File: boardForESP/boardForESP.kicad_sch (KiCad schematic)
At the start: 6 parts, among them J1 Conn_01x15_Socket, J2 Conn_01x15_Socket

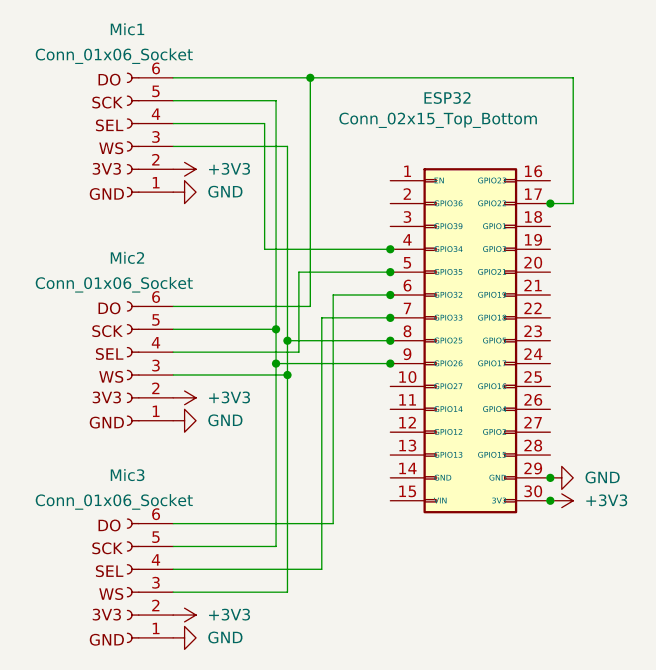
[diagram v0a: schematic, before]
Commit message: Refactor schematic and PCB files, update audio topic, and optimize MQTT data handling
- Removed unnecessary junctions in the KiCad schematic for clarity.
- Added new junctions to improve circuit connections.
- Updated wire connections to reflect the latest design changes.
- Deleted the lock file for the PCB to prevent conflicts.
- Changed MQTT audio topic from "I2S1" to "I2S0" for consistency.
- Modified MQTT data handling in `mqqtInterface.py` to skip every other sample for better performance.
- Updated binary files `debug_mel.npy` and `output.wav` to reflect recent changes.
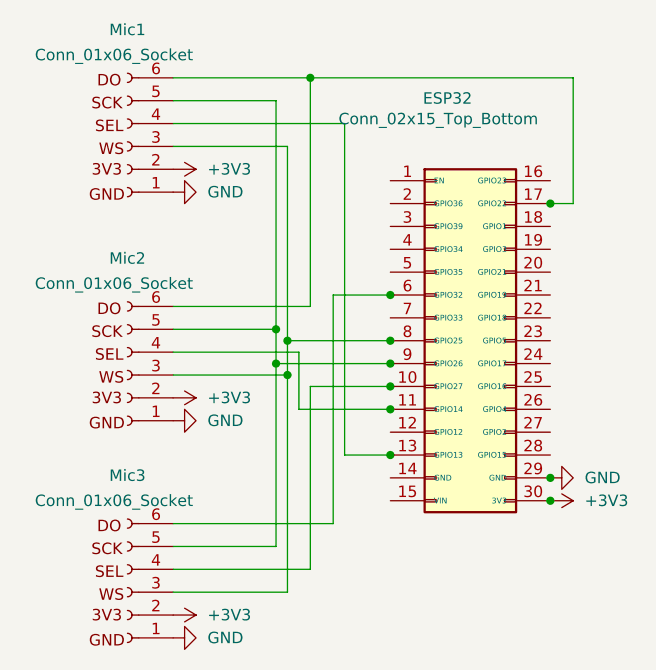
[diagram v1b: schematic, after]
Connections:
- net at ESP32.4 (GPIO34), J1.12 (Pin_12): no longer Mic1.4 (Pin_4)
- net at ESP32.5 (GPIO35), J1.11 (Pin_11): no longer Mic2.4 (Pin_4)
- net at ESP32.10 (GPIO27), J1.6 (Pin_6): now also Mic3.4 (Pin_4)
- net at ESP32.11 (GPIO14), J1.5 (Pin_5): now also Mic2.4 (Pin_4)
- net at ESP32.13 (GPIO13), J1.3 (Pin_3): now also Mic1.4 (Pin_4)
- net at ESP32.7 (GPIO33), J1.9 (Pin_9): no longer Mic3.4 (Pin_4)
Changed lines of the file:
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@@
-	)
-	(junction
-		(at 123.19 113.03)
-		(diameter 0)
-		(color 0 0 0 0)
-	)
-	(junction
-		(at 123.19 118.11)
-		(diameter 0)
-		(color 0 0 0 0)
 	)
 	(junction
@@
 	)
 	(junction
+		(at 123.19 133.35)
+		(diameter 0)
+		(color 0 0 0 0)
+	)
+	(junction
 		(at 111.76 124.46)
 		(diameter 0)
@@
 	)
 	(junction
-		(at 123.19 110.49)
+		(at 123.19 125.73)
+		(diameter 0)
+		(color 0 0 0 0)
+	)
+	(junction
+		(at 123.19 128.27)
 		(diameter 0)
 		(color 0 0 0 0)
@@
 	(wire
 		(pts
+			(xy 118.11 133.35) (xy 123.19 133.35)
+		)
+		(stroke
+			(width 0)
+			(type default)
+		)
+	)
+	(wire
+		(pts
 			(xy 99.06 124.46) (xy 111.76 124.46)
 		)
@@
 	(wire
 		(pts
-			(xy 99.06 146.05) (xy 115.57 146.05)
-		)
-		(stroke
-			(width 0)
-			(type default)
-		)
-	)
-	(wire
-		(pts
 			(xy 110.49 119.38) (xy 110.49 123.19)
 		)
@@
 	(wire
 		(pts
-			(xy 109.22 96.52) (xy 109.22 110.49)
-		)
-		(stroke
-			(width 0)
-			(type default)
-		)
-	)
-	(wire
-		(pts
 			(xy 99.06 93.98) (xy 110.49 93.98)
 		)
@@
 	(wire
 		(pts
+			(xy 118.11 96.52) (xy 118.11 133.35)
+		)
+		(stroke
+			(width 0)
+			(type default)
+		)
+	)
+	(wire
+		(pts
+			(xy 99.06 121.92) (xy 113.03 121.92)
+		)
+		(stroke
+			(width 0)
+			(type default)
+		)
+	)
+	(wire
+		(pts
 			(xy 111.76 120.65) (xy 123.19 120.65)
 		)
@@
 	(wire
 		(pts
-			(xy 113.03 121.92) (xy 113.03 113.03)
-		)
-		(stroke
-			(width 0)
-			(type default)
-		)
-	)
-	(wire
-		(pts
 			(xy 111.76 124.46) (xy 111.76 120.65)
 		)
@@
 	(wire
 		(pts
-			(xy 109.22 110.49) (xy 123.19 110.49)
+			(xy 99.06 96.52) (xy 118.11 96.52)
 		)
 		(stroke
@@
 	(wire
 		(pts
-			(xy 115.57 146.05) (xy 115.57 118.11)
+			(xy 113.03 121.92) (xy 113.03 128.27)
 		)
 		(stroke
@@
 	(wire
 		(pts
-			(xy 113.03 113.03) (xy 123.19 113.03)
-		)
-		(stroke
-			(width 0)
-			(type default)
-		)
-	)
-	(wire
-		(pts
-			(xy 99.06 96.52) (xy 109.22 96.52)
-		)
-		(stroke
-			(width 0)
-			(type default)
-		)
-	)
-	(wire
-		(pts
 			(xy 99.06 99.06) (xy 111.76 99.06)
 		)
@@
 	(wire
 		(pts
-			(xy 99.06 121.92) (xy 113.03 121.92)
-		)
-		(stroke
-			(width 0)
-			(type default)
-		)
-	)
-	(wire
-		(pts
 			(xy 116.84 140.97) (xy 116.84 115.57)
 		)
@@
 	(wire
 		(pts
+			(xy 99.06 146.05) (xy 114.3 146.05)
+		)
+		(stroke
+			(width 0)
+			(type default)
+		)
+	)
+	(wire
+		(pts
+			(xy 114.3 125.73) (xy 123.19 125.73)
+		)
+		(stroke
+			(width 0)
+			(type default)
+		)
+	)
+	(wire
+		(pts
 			(xy 111.76 148.59) (xy 111.76 124.46)
 		)
@@
 	(wire
 		(pts
-			(xy 115.57 118.11) (xy 123.19 118.11)
-		)
-		(stroke
-			(width 0)
-			(type default)
-		)
-	)
-	(wire
-		(pts
 			(xy 99.06 119.38) (xy 110.49 119.38)
 		)
 		(stroke
+			(width 0)
+			(type default)
+		)
+	)
+	(wire
+		(pts
+			(xy 114.3 146.05) (xy 114.3 125.73)
+		)
+		(stroke
+			(width 0)
+			(type default)
+		)
+	)
+	(wire
+		(pts
+			(xy 113.03 128.27) (xy 123.19 128.27)
+		)
+		(stroke

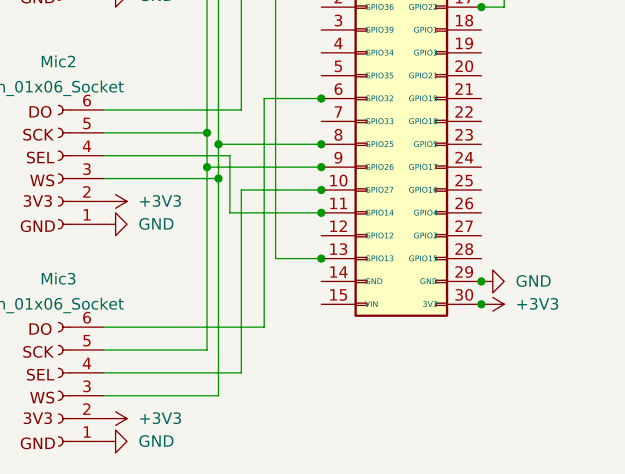
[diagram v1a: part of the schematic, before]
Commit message: Refactor junctions and wires in the schematic for improved connectivity and layout. Added new junctions at specified coordinates and updated wire connections accordingly. Removed redundant junction and adjusted UUIDs for consistency. Created a lock file for PCB design to prevent concurrent modifications.
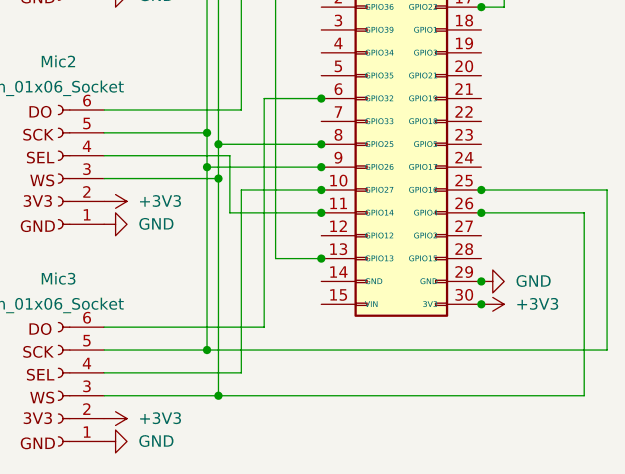
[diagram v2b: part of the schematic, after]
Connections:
- net at ESP32.8 (GPIO25), J1.8 (Pin_8), Mic1.3 (Pin_3)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: now also ESP32.26 (GPIO4), J2.5 (Pin_5)
- net at ESP32.9 (GPIO26), J1.7 (Pin_7), Mic1.5 (Pin_5)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: now also ESP32.25 (GPIO16), J2.6 (Pin_6)
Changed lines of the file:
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@@
+	)
+	(junction
+		(at 114.3 91.44)
+		(diameter 0)
+		(color 0 0 0 0)
+	)
+	(junction
+		(at 123.19 115.57)
+		(diameter 0)
+		(color 0 0 0 0)
+	)
+	(junction
+		(at 140.97 128.27)
+		(diameter 0)
+		(color 0 0 0 0)
+	)
+	(junction
+		(at 123.19 120.65)
+		(diameter 0)
+		(color 0 0 0 0)
+	)
+	(junction
+		(at 110.49 119.38)
+		(diameter 0)
+		(color 0 0 0 0)
+	)
+	(junction
+		(at 140.97 125.73)
+		(diameter 0)
+		(color 0 0 0 0)
+	)
+	(junction
+		(at 123.19 133.35)
+		(diameter 0)
+		(color 0 0 0 0)
+	)
+	(junction
+		(at 111.76 148.59)
+		(diameter 0)
+		(color 0 0 0 0)
+	)
+	(junction
+		(at 111.76 124.46)
+		(diameter 0)
+		(color 0 0 0 0)
+	)
+	(junction
+		(at 111.76 120.65)
+		(diameter 0)
+		(color 0 0 0 0)
+	)
+	(junction
+		(at 140.97 135.89)
+		(diameter 0)
+		(color 0 0 0 0)
+	)
+	(junction
+		(at 123.19 125.73)
+		(diameter 0)
+		(color 0 0 0 0)
+	)
+	(junction
+		(at 123.19 128.27)
+		(diameter 0)
+		(color 0 0 0 0)
 	)
 	(junction
@@
 	)
 	(junction
-		(at 114.3 91.44)
-		(diameter 0)
-		(color 0 0 0 0)
-	)
-	(junction
-		(at 123.19 115.57)
-		(diameter 0)
-		(color 0 0 0 0)
-	)
-	(junction
-		(at 123.19 120.65)
-		(diameter 0)
-		(color 0 0 0 0)
-	)
-	(junction
-		(at 110.49 119.38)
-		(diameter 0)
-		(color 0 0 0 0)
-	)
-	(junction
-		(at 123.19 133.35)
-		(diameter 0)
-		(color 0 0 0 0)
-	)
-	(junction
-		(at 111.76 124.46)
-		(diameter 0)
-		(color 0 0 0 0)
-	)
-	(junction
-		(at 111.76 120.65)
-		(diameter 0)
-		(color 0 0 0 0)
-	)
-	(junction
-		(at 140.97 135.89)
-		(diameter 0)
-		(color 0 0 0 0)
-	)
-	(junction
-		(at 123.19 125.73)
-		(diameter 0)
-		(color 0 0 0 0)
-	)
-	(junction
-		(at 123.19 128.27)
+		(at 110.49 143.51)
 		(diameter 0)
 		(color 0 0 0 0)
@@
 	(wire
 		(pts
+			(xy 154.94 143.51) (xy 154.94 125.73)
+		)
+		(stroke
+			(width 0)
+			(type default)
+		)
+	)
+	(wire
+		(pts
+			(xy 110.49 143.51) (xy 154.94 143.51)
+		)
+		(stroke
+			(width 0)
+			(type default)
+		)
+	)
+	(wire
+		(pts
 			(xy 99.06 93.98) (xy 110.49 93.98)
 		)
@@
 	(wire
 		(pts
+			(xy 110.49 123.19) (xy 110.49 143.51)
+		)
+		(stroke
+			(width 0)
+			(type default)
+		)
+	)
+	(wire
+		(pts
+			(xy 111.76 124.46) (xy 111.76 148.59)
+		)
+		(stroke
+			(width 0)
+			(type default)
+		)
+	)
+	(wire
+		(pts
 			(xy 111.76 124.46) (xy 111.76 120.65)
 		)
@@
 	(wire
 		(pts
-			(xy 110.49 143.51) (xy 110.49 123.19)
-		)
-		(stroke
-			(width 0)
-			(type default)
-		)
-	)
-	(wire
-		(pts
 			(xy 99.06 96.52) (xy 118.11 96.52)
 		)
@@
 	(wire
 		(pts
+			(xy 154.94 125.73) (xy 140.97 125.73)
+		)
+		(stroke
+			(width 0)
+			(type default)
+		)
+	)
+	(wire
+		(pts
 			(xy 99.06 146.05) (xy 114.3 146.05)
 		)
@@
 	(wire
 		(pts
-			(xy 111.76 148.59) (xy 111.76 124.46)
-		)
-		(stroke
-			(width 0)
-			(type default)
-		)
-	)
-	(wire
-		(pts
 			(xy 114.3 91.44) (xy 143.51 91.44)
 		)
@@
 	(wire
 		(pts
+			(xy 111.76 148.59) (xy 152.4 148.59)
+		)
+		(stroke
+			(width 0)
+			(type default)
+		)
+	)
+	(wire
+		(pts
 			(xy 113.03 128.27) (xy 123.19 128.27)
 		)
@@
 		)
 		(stroke
+			(width 0)
+			(type default)
+		)
+	)
+	(wire
+		(pts
+			(xy 152.4 148.59) (xy 152.4 128.27)
+		)
+		(stroke
+			(width 0)
+			(type default)
+		)
+	)
+	(wire
+		(pts
+			(xy 152.4 128.27) (xy 140.97 128.27)
+		)
+		(stroke

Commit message: not sure about this
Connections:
- net +3V3: no longer ESP32.30 (3V3), J2.1 (Pin_1)
- new net: ESP32.30 (3V3), J2.1 (Pin_1)
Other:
- title: (none) -> ESP32 and 3 I2S microphones
- moved on the sheet: ESP32, Mic1, Mic2, Mic3

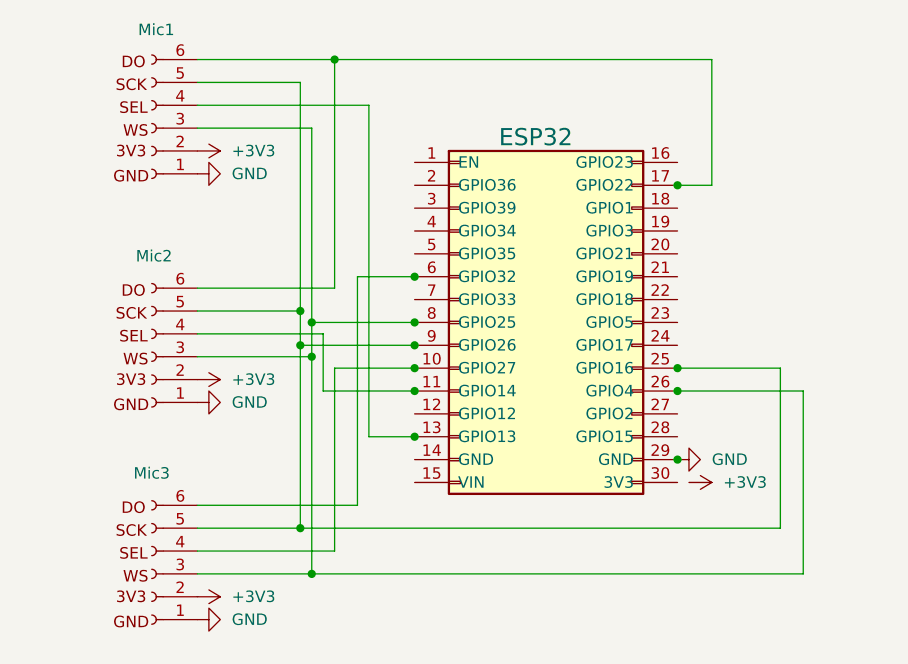
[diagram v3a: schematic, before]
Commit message: Update MQTT server configuration and disable GPU usage
- Changed MQTT_SERVER from "10.250.34.201" to "192.168.1.20"
- Disabled GPU usage by setting USE_GPU to False
- Disabled plotting by setting SHOULD_PLOT to False
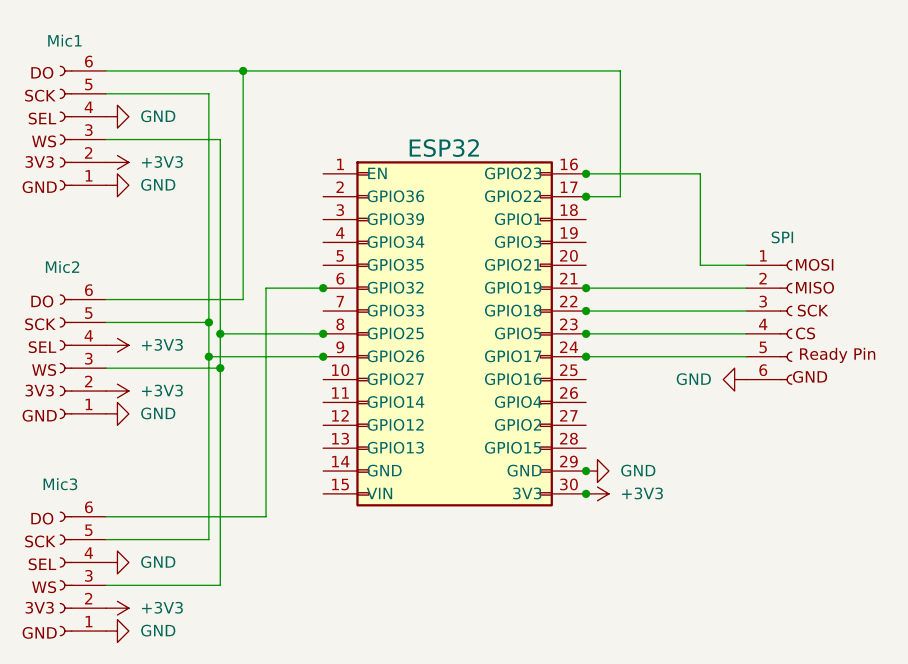
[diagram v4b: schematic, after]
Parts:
- added SPI: Conn_01x06_Socket, Connector_PinSocket_2.54mm:PinSocket_1x06_P2.54mm_Vertical, symbol Connector:Conn_01x06_Socket
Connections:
- net +3V3: now also ESP32.30 (3V3), J2.1 (Pin_1), Mic2.4 (Pin_4)
- net GND: now also Mic1.4 (Pin_4), Mic3.4 (Pin_4), SPI.6 (Pin_6)
- net at ESP32.8 (GPIO25), J1.8 (Pin_8), Mic1.3 (Pin_3)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: no longer ESP32.26 (GPIO4), J2.5 (Pin_5)
- net at ESP32.13 (GPIO13), J1.3 (Pin_3): no longer Mic1.4 (Pin_4)
- net at ESP32.9 (GPIO26), J1.7 (Pin_7), Mic1.5 (Pin_5)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: no longer ESP32.25 (GPIO16), J2.6 (Pin_6)
- net at ESP32.11 (GPIO14), J1.5 (Pin_5): no longer Mic2.4 (Pin_4)
- net at ESP32.10 (GPIO27), J1.6 (Pin_6): no longer Mic3.4 (Pin_4)
- net at ESP32.16 (GPIO23), J2.15 (Pin_15): now also SPI.1 (Pin_1)
- net at ESP32.21 (GPIO19), J2.10 (Pin_10): now also SPI.2 (Pin_2)
- net at ESP32.22 (GPIO18), J2.9 (Pin_9): now also SPI.3 (Pin_3)
- net at ESP32.23 (GPIO5), J2.8 (Pin_8): now also SPI.4 (Pin_4)
- net at ESP32.24 (GPIO17), J2.7 (Pin_7): now also SPI.5 (Pin_5)
- new net: ESP32.25 (GPIO16), J2.6 (Pin_6)
- new net: ESP32.26 (GPIO4), J2.5 (Pin_5)
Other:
- moved on the sheet: ESP32, Mic1, Mic2, Mic3
